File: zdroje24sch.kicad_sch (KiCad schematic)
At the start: 8 parts, among them J2 Conn_02x05_Top_Bottom

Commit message: Zapojit vse.
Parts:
- added CB3, CB4, CB5, CB6: H8500VBBB076W, symbol Device:CircuitBreaker_1P
- added D2, D3, D4, D5: IND8-12G-B, symbol Device:LED
- added F2, F3: 4 A, symbol Device:Fuse
- added F4: 6.2 A, symbol Device:Fuse
- added F5: 3 A, symbol Device:Fuse
- added F6: 4 A slow, symbol Device:Fuse
- added LA1: ~, symbol Device:Lamp
- added MES2, MES3: ~, symbol Device:Ammeter_DC
- added PS1: LRS-150-12, Converter_ACDC:Converter_ACDC_Murata_BAC05SxxDC_THT, symbol Converter_ACDC:BAC05S05DC
- added PS2: LRS-150-24, Converter_ACDC:Converter_ACDC_Murata_BAC05SxxDC_THT, symbol Converter_ACDC:BAC05S05DC
- added PS3: LRS-50-15, Converter_ACDC:Converter_ACDC_Murata_BAC05SxxDC_THT, symbol Converter_ACDC:BAC05S05DC
- CB1: value CircuitBreaker_2P -> IRS-201-1C3-G/B
- CB2: value CircuitBreaker_1P -> H8500VBBB076W
- D1: value LED -> IND8-12G-B
- F1: value Fuse -> 6.2 A; Pouzdro (none) -> LS-506
- J1: value ~ -> FBNAB2470ZG110
- J2: value Conn_02x05_Top_Bottom -> ~
- MES1: value Ammeter_DC -> ~
- N1: value Housing_Pad -> ~
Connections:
- net at N1.1 (PAD): now also J1.3 (PE)
- net GND: now reaches J2.1 (Pin_1)
- net GND: now also D1.1 (K), J2.7 (Pin_7), J2.9 (Pin_9), D2.1 (K), D3.1 (K), PS1.4 (-Vo)
- net BOOST-: now reaches J2.10 (Pin_10)
- net BOOST-: now also D4.1 (K), PS2.4 (-Vo)
- net ACC: now reaches J2.2 (Pin_2)
- net ACC: now also D3.2 (A), F3.2
- net DSC: now reaches J2.3 (Pin_3)
- net DSC: now also D5.2 (A), F5.2
- net SWITCH: now reaches J2.4 (Pin_4)
- net SWITCH: now also D1.2 (A), F1.2
- net BOOST+: now reaches J2.5 (Pin_5)
- net BOOST+: now also D4.2 (A), F4.2
- net MTB: now reaches J2.6 (Pin_6)
- net MTB: now also D2.2 (A), F2.2
- net GND-DSC: now reaches J2.8 (Pin_8)
- net GND-DSC: now also D5.1 (K), PS3.4 (-Vo)
- net at CB2.1: now also F1.1
- net at CB2.2: now also MES1.1 (-), CB3.2, CB4.2
- net at CB1.1: now also F6.1, LA1.1 (-)
- net at CB1.2: now also J1.1 (L)
- net at CB1.3: now also LA1.2 (+), PS1.1 (AC/N), PS2.1 (AC/N), PS3.1 (AC/N)
- net at CB1.4: now also J1.2 (N)
- net at MES1.2 (+): now also PS1.5 (+Vo)
- new net: CB5.1, F4.1
- new net: CB6.1, F5.1
- new net: CB6.2, MES3.1 (-)
- new net: CB3.1, F2.1
- new net: F6.2, PS1.2 (AC/L), PS2.2 (AC/L), PS3.2 (AC/L)
- new net: CB4.1, F3.1
- new net: MES2.2 (+), PS2.5 (+Vo)
- new net: CB5.2, MES2.1 (-)
- new net: MES3.2 (+), PS3.5 (+Vo)
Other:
- note added: "Doutnavka LA1 je součástí spínače CB1"
- note added: "Napájet přímo z výstupu PS1"
- note added: "Napájet přímo z výstupu PS2"
- note added: "Napájet přímo z výstupu PS3"
- note added: "Omezení pro návrh: * Indikační LED musí být za pojistkou (aby indikovala stav pojistky). * Tlačítko by nejspíš mělo být před pojistkou (aby se dala měnit pojistka za vypnutého zdroje)."
- note added: "Síťový filtr je součástí J1"
- title: (none) -> Napájecí zdroj KMŽ/LRKV 2024/2025
- moved on the sheet: CB1, CB2, D1, F1, J1, J2, MES1, N1

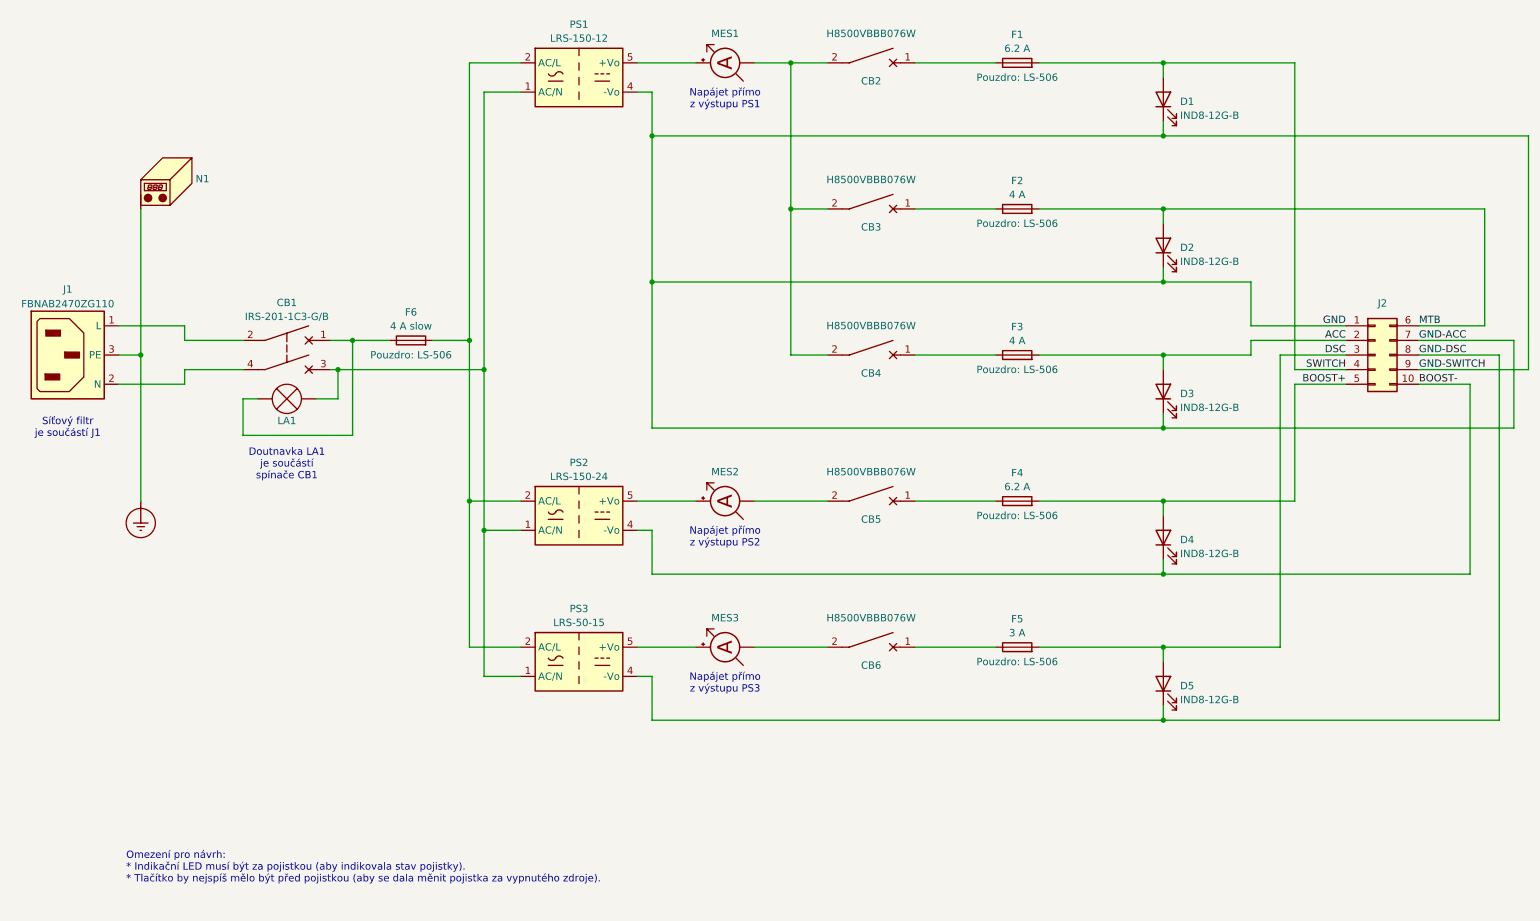
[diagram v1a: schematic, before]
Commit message: Vstupni pojistka pred vstupnim tlacitkem.
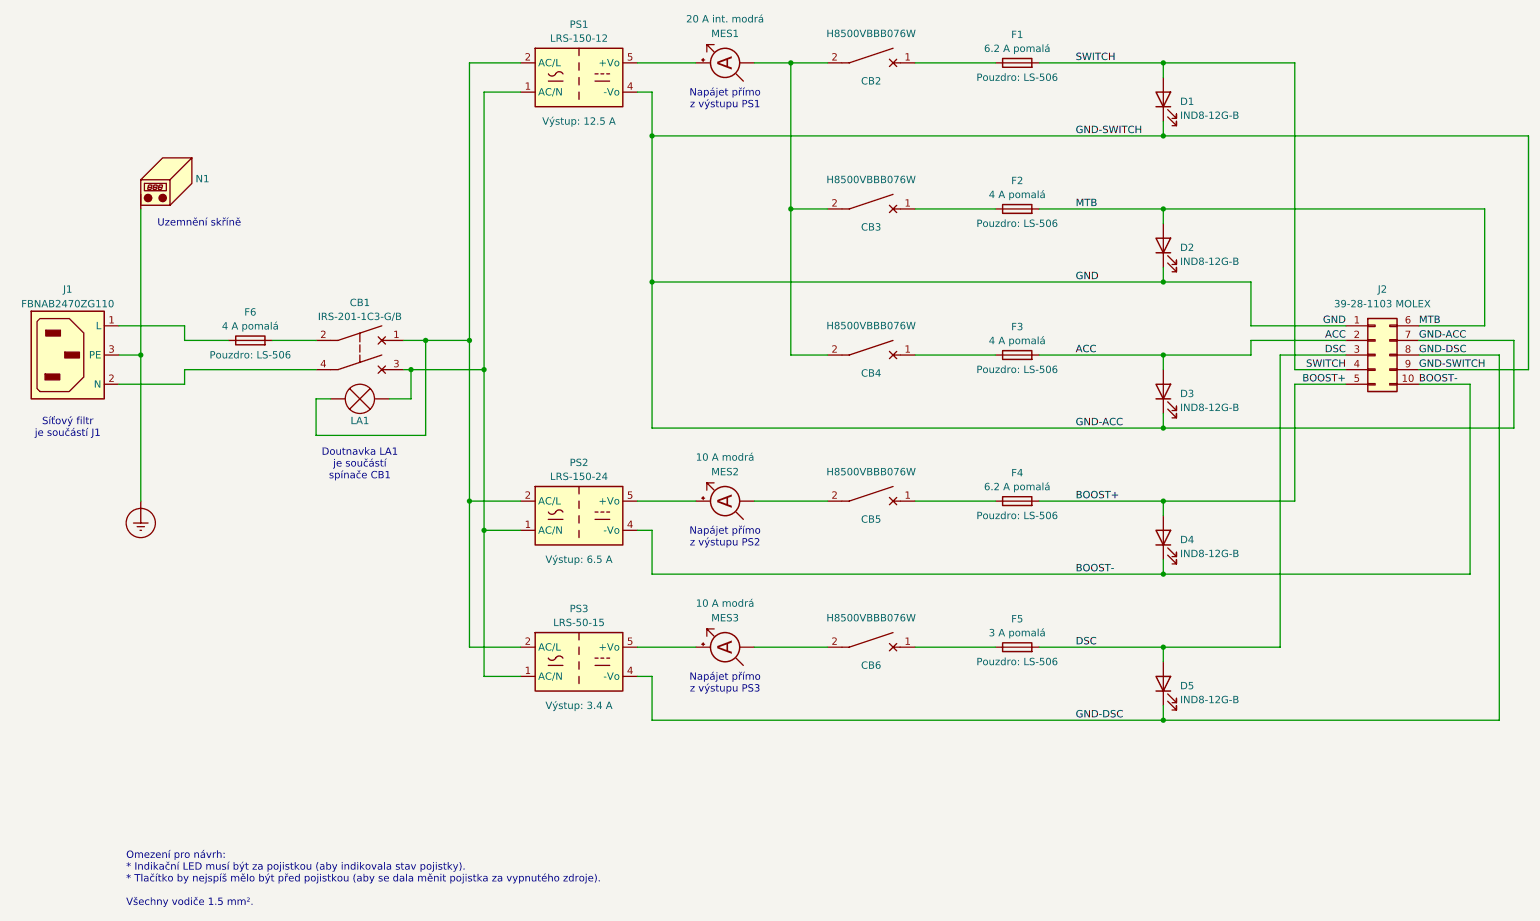
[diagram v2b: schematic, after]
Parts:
- F1, F4: value 6.2 A -> 6.2 A pomalá
- F2, F3: value 4 A -> 4 A pomalá
- F5: value 3 A -> 3 A pomalá
- F6: value 4 A slow -> 4 A pomalá
- J2: value ~ -> 39-28-1103 MOLEX
- MES1: value ~ -> 20 A int. modrá
- MES2, MES3: value ~ -> 10 A modrá
- PS1: Výstup (none) -> 12.5 A
- PS2: Výstup (none) -> 6.5 A
- PS3: Výstup (none) -> 3.4 A
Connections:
- net at CB1.1, LA1.1 (-): now also PS1.2 (AC/L), PS2.2 (AC/L), PS3.2 (AC/L); no longer F6.1
- net at J1.1 (L): now also F6.1; no longer CB1.2
- new net: CB1.2, F6.2
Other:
- note added: "Omezení pro návrh: * Indikační LED musí být za pojistkou (aby indikovala stav pojistky). * Tlačítko by nejspíš mělo být před pojistkou (aby se dala měnit pojistka za vypnutého zdroje). Všechny vodiče 1.5 mm²."
- note added: "Uzemnění skříně"
- note removed: "Omezení pro návrh: * Indikační LED musí být za pojistkou (aby indikovala stav pojistky). * Tlačítko by nejspíš mělo být před pojistkou (aby se dala měnit pojistka za vypnutého zdroje)."
- company: (none) -> Jan Horáček, Miroslav Horáček
- title: Napájecí zdroj KMŽ/LRKV 2024/2025 -> Napájecí zdroj kolejišť KMŽ/LRKV 2024/2025
- moved on the sheet: CB1, F6, LA1

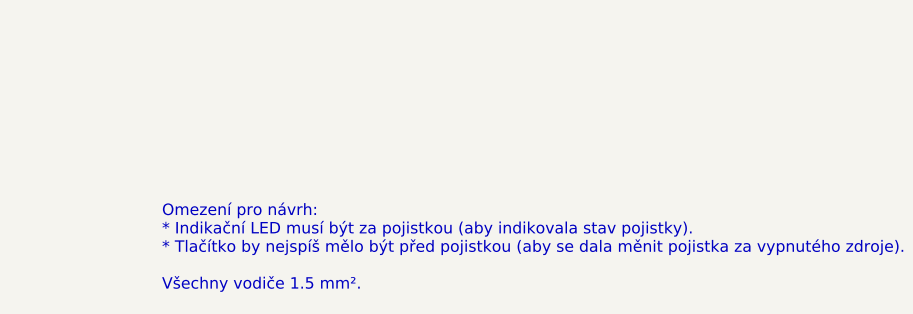
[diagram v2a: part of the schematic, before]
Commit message: Prurez vsech lanek 1.0 mm2.
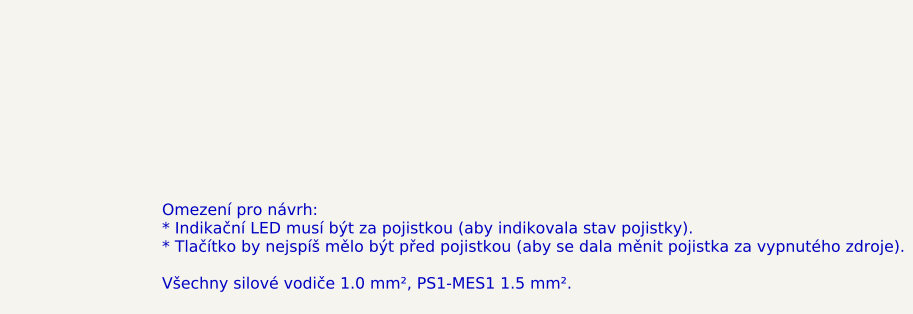
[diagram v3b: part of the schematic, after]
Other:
- note added: "Omezení pro návrh: * Indikační LED musí být za pojistkou (aby indikovala stav pojistky). * Tlačítko by nejspíš mělo být před pojistkou (aby se dala měnit pojistka za vypnutého zdroje). Všechny silové vodiče 1.0 mm², PS1-MES1 1.5 mm²."
- note removed: "Omezení pro návrh: * Indikační LED musí být za pojistkou (aby indikovala stav pojistky). * Tlačítko by nejspíš mělo být před pojistkou (aby se dala měnit pojistka za vypnutého zdroje). Všechny vodiče 1.5 mm²."
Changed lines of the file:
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@@
 	(title_block
 		(title "Napájecí zdroj kolejišť KMŽ/LRKV 2024/2025")
-		(date "2024-12-24")
+		(date "2025-01-01")
 		(rev "1.0")
 		(company "Jan Horáček, Miroslav Horáček")
@@
 		)
 	)
-	(text "Omezení pro návrh:\n* Indikační LED musí být za pojistkou (aby indikovala stav pojistky).\n* Tlačítko by nejspíš mělo být před pojistkou (aby se dala měnit pojistka za vypnutého zdroje).\n\nVšechny vodiče 1.5 mm²."
+	(text "Omezení pro návrh:\n* Indikační LED musí být za pojistkou (aby indikovala stav pojistky).\n* Tlačítko by nejspíš mělo být před pojistkou (aby se dala měnit pojistka za vypnutého zdroje).\n\nVšechny silové vodiče 1.0 mm², PS1-MES1 1.5 mm²."
 		(exclude_from_sim no)
 		(at 35.56 175.26 0)
